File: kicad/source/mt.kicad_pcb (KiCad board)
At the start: 4 copper layers, 132 parts, among them IC1 MCP73831T-2ACI_OT, IC10 SN74HC148NSR, IC11 SN74HC148NSR, IC2 BQ29728DSER, IC3 TLV74333PDBVR, IC4 TLV9152IDR, IC5 MSPM0G3507SPMR, IC6 IS62WV1288BLL-55QLI, IC7 DAC082S085CIMMX_NOPB, IC8 SN74HC148NSR, IC9 SN74HC148NSR, J1 694106301002, J2 3557-2, J3 SJ1-3524N, J4 Conn_01x05_Pin, J5 Conn_01x09_Pin, J6 Conn_01x03_Pin, J7 Conn_01x03_Pin, J8 Conn_01x03_Pin, Q1 CSD16406Q3, Q2 CSD16406Q3, U1 1043

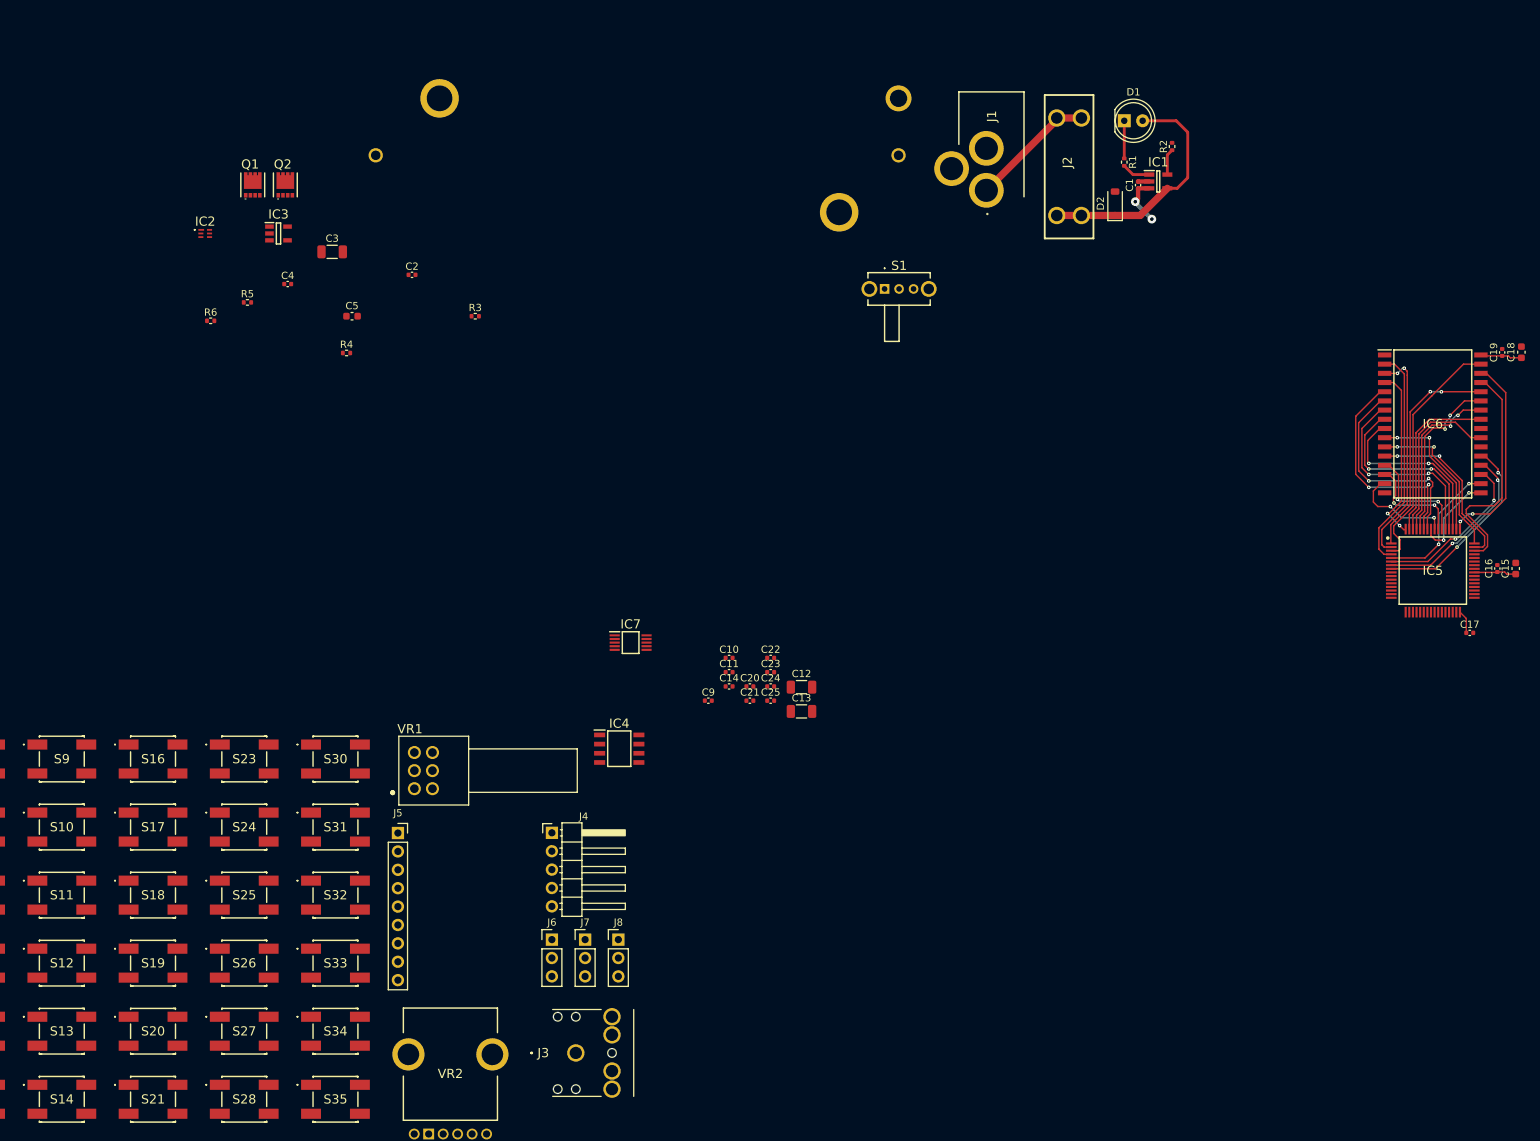
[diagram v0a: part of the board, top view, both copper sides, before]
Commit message: completed power electronics routing, fixed battery holder model
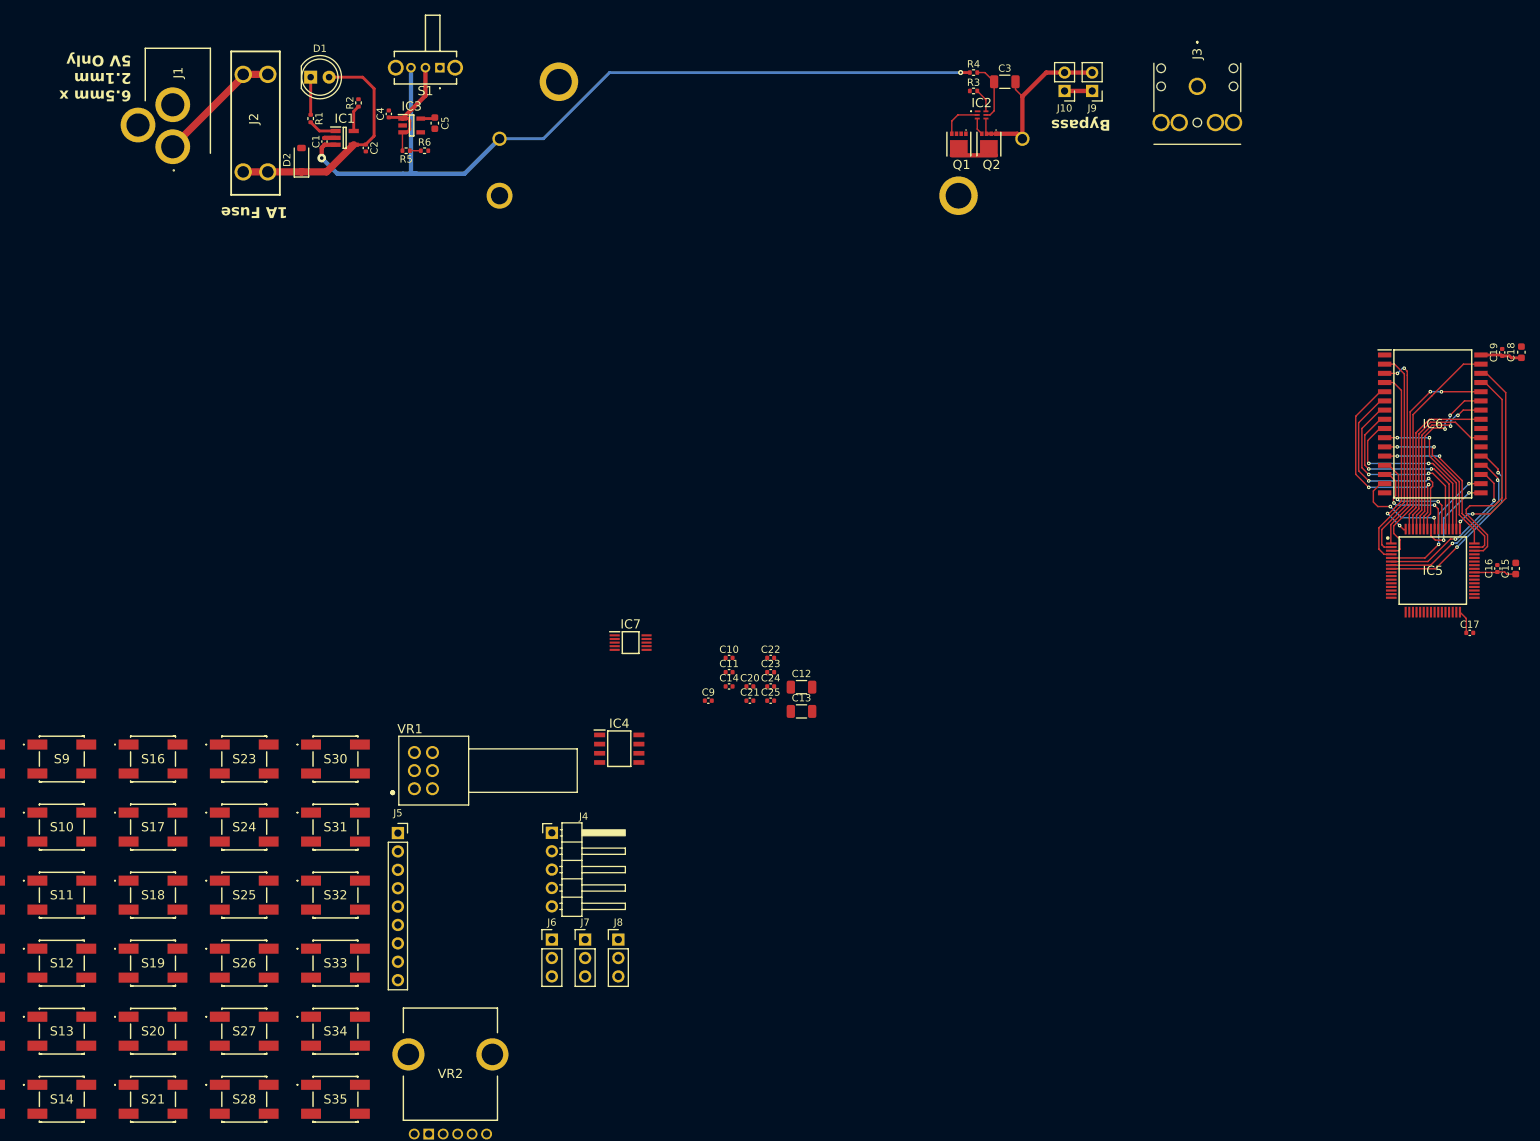
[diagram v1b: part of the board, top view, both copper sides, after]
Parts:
- added J10: Conn_01x02_Pin, Connector_PinHeader_2.54mm:PinHeader_1x02_P2.54mm_Vertical, F.Cu at (180.3, 23.5)
- added J9: Conn_01x02_Pin, Connector_PinHeader_2.54mm:PinHeader_1x02_P2.54mm_Vertical, F.Cu at (184.2, 23.5)
- moved J3 158.7 mm to (198.7, 22.9), turned to -90 degrees
- moved J1 112.5 mm to (53.4, 17.6)
- moved C1 112.5 mm to (78.1, 30.5)
- moved D1 112.5 mm to (76.2, 21.6)
- moved J2 112.5 mm to (68.6, 27.9)
- moved R1 112.5 mm to (76.2, 27.3)
- moved D2 112.5 mm to (74.9, 33.0)
- moved IC1 112.5 mm to (80.9, 30.0)
- moved R2 112.5 mm to (82.8, 25.1)
- moved IC2 108.5 mm to (168.9, 26.8)
- moved Q1 97.7 mm to (165.7, 30.8), turned to 180 degrees
- moved Q2 97.3 mm to (169.9, 30.8), turned to 180 degrees
- moved C3 95.8 mm to (172.1, 22.2)
- moved R4 94.9 mm to (167.8, 21.0)
- moved R3 75.5 mm to (167.8, 23.5)
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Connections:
- Q1 pad 9: Net-(Q1-D_1) -> (no net)
- Q2 pad 9: Net-(Q1-D_1) -> (no net)
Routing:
- net CELL+: track 6.88 -> 115.1 mm
- net Net-(IC2-VSS): track 0.00 -> 26.6 mm
- net Net-(IC3-EN): track 0.00 -> 16.4 mm
- net Net-(IC2-BAT): track 0.00 -> 8.25 mm
- net Net-(Q1-D_1): track 0.00 -> 6.10 mm
- net Net-(IC2-COUT): track 0.00 -> 5.62 mm
- net GND: track 1.56 -> 5.37 mm
- net Net-(IC2-V-): track 0.00 -> 3.31 mm
- net Net-(IC2-DOUT): track 0.00 -> 2.36 mm
- net VDD: track 11.6 -> 13.8 mm
- net VBAT: track 0.00 -> 1.52 mm
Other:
- board text added: "1A Fuse"
- board text added: "6.5mm x 2.1mm 5V Only"
- board text added: "Bypass"

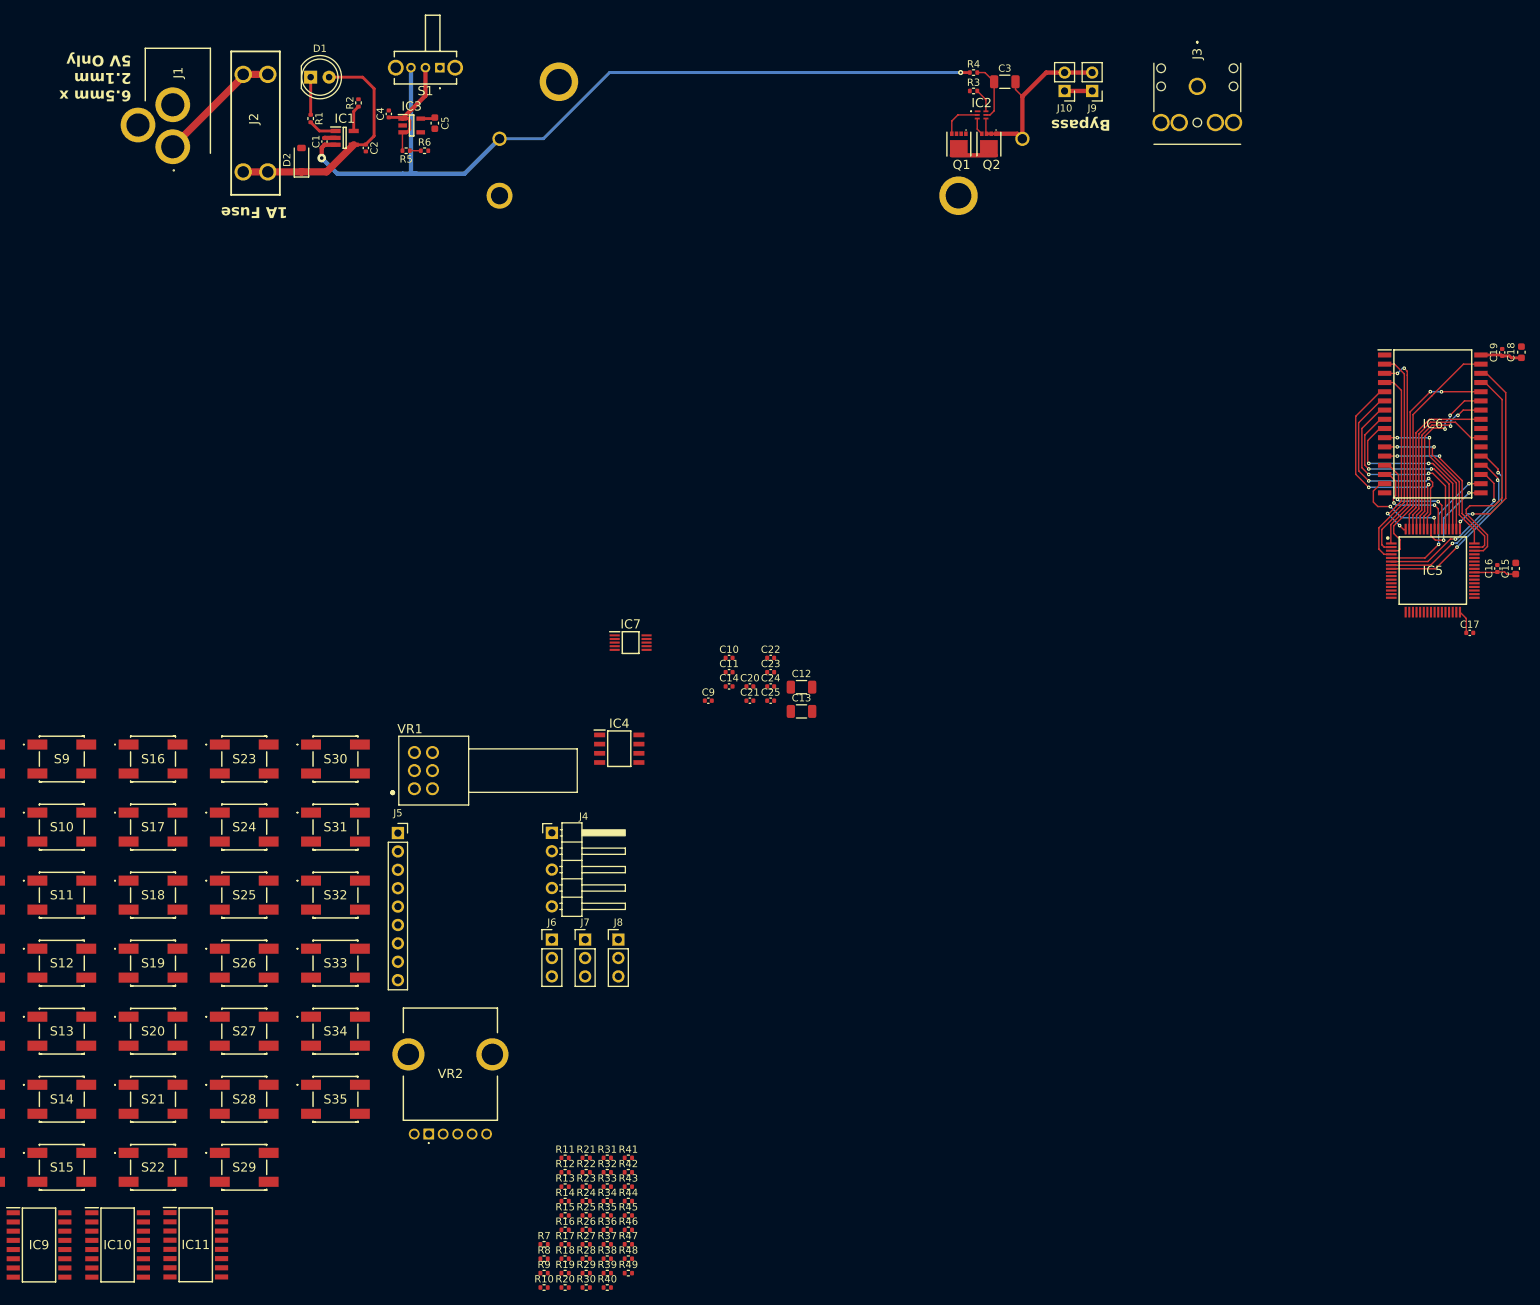
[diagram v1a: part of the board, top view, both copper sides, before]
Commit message: completed analog electronics routing
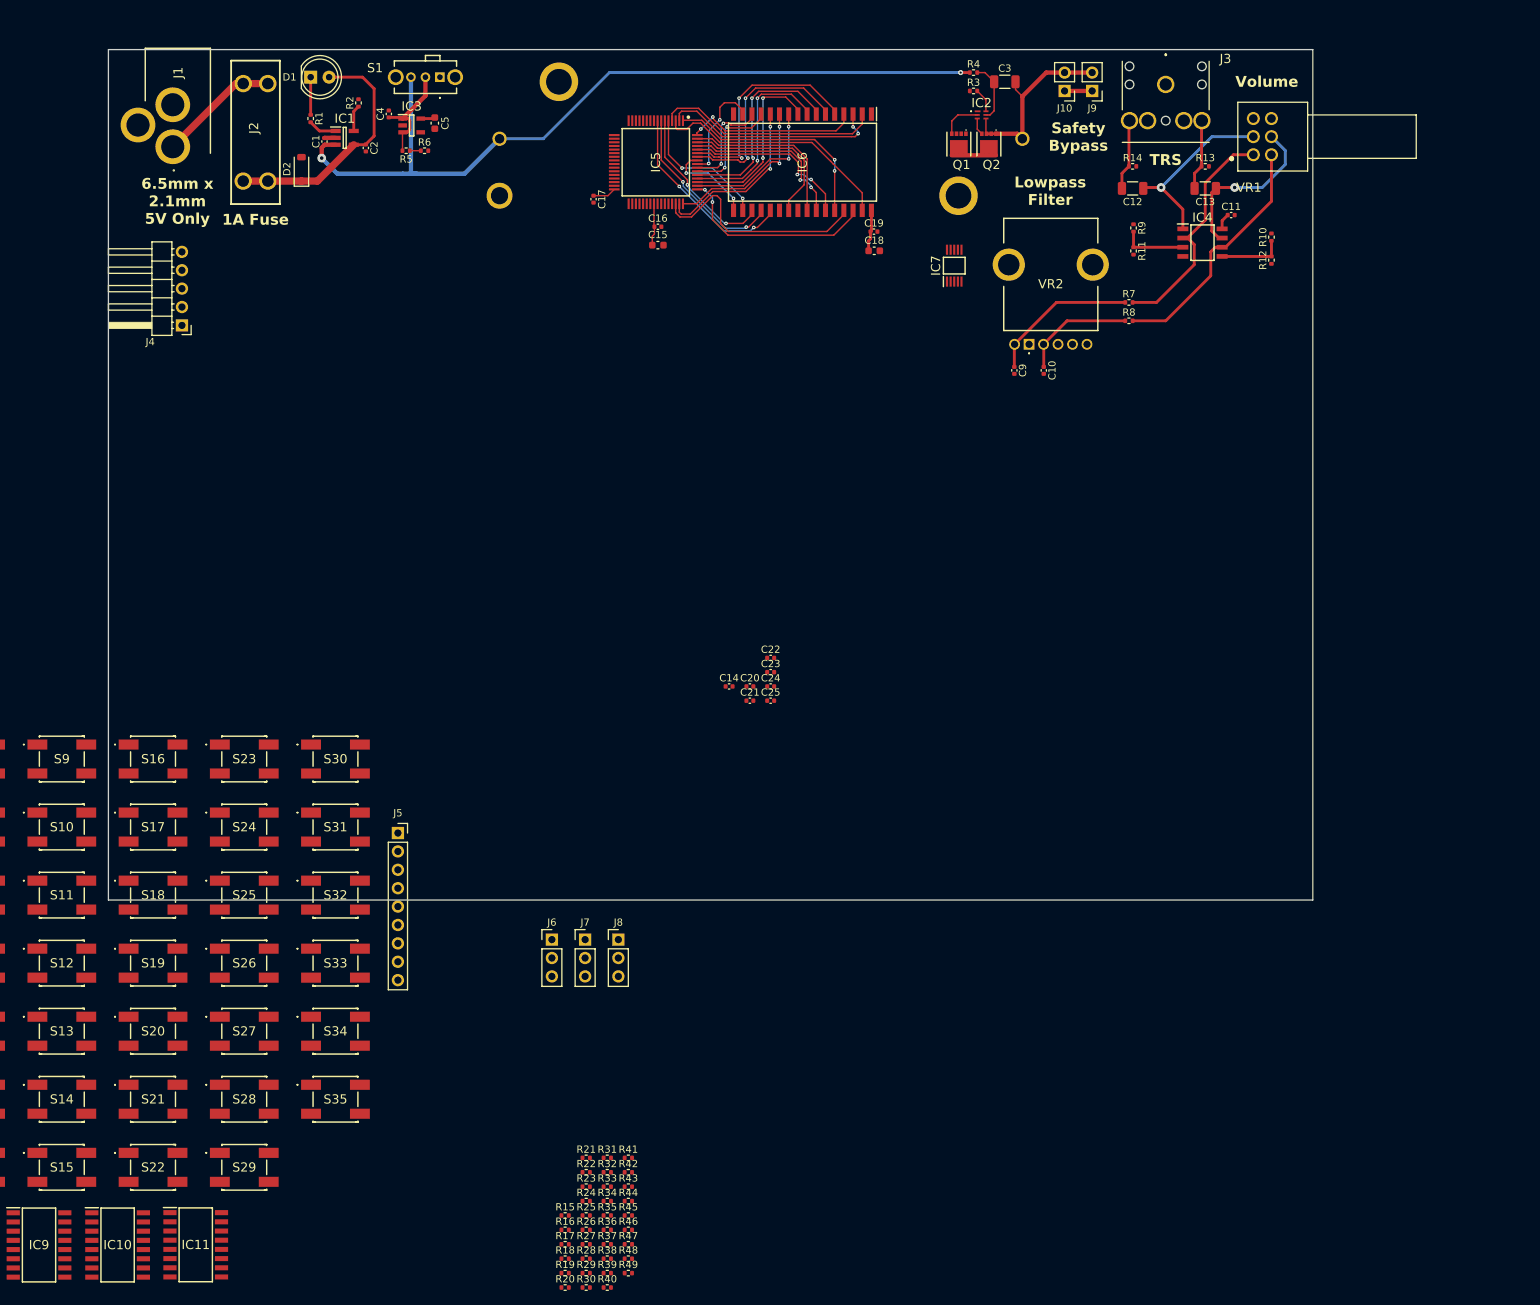
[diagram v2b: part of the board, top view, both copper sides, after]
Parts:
- moved R10 176.5 mm to (208.9, 43.7), turned to 90 degrees
- moved R13 166.4 mm to (199.8, 33.9)
- moved R9 165.8 mm to (189.9, 42.4), turned to -90 degrees
- moved R14 163.0 mm to (189.7, 33.9)
- moved R12 159.4 mm to (208.9, 46.9), turned to 90 degrees
- moved R7 153.1 mm to (189.2, 52.7)
- moved R8 152.7 mm to (189.2, 55.2)
- moved R11 147.8 mm to (189.9, 45.6), turned to -90 degrees
- moved VR1 145.3 mm to (206.4, 32.3)
- moved VR2 137.0 mm to (175.4, 58.5)
- moved C17 135.1 mm to (115.3, 38.4), turned to -90 degrees
- moved C15 126.6 mm to (124.2, 44.8), turned to 0 degrees
- moved C16 125.2 mm to (124.2, 42.3), turned to 0 degrees
- moved IC5 121.3 mm to (123.9, 33.3), turned to -90 degrees
- moved IC4 106.7 mm to (199.4, 44.5)
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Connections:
- R12 pad 1: Net-(IC4-IN2+) -> GND
- R12 pad 2: GND -> Net-(IC4-IN2+)
- R7 pad 1: RV1A -> Net-(C9-Pad1)
- R7 pad 2: Net-(C9-Pad1) -> RV1A
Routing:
- net RV2A: track 0.00 -> 34.4 mm
- net RV1A: track 0.00 -> 32.9 mm
- net L: track 0.00 -> 25.1 mm, vias 0 -> 1
- net R: track 0.00 -> 23.5 mm, vias 0 -> 1
- net Net-(C9-Pad1): track 0.00 -> 20.8 mm
- net Net-(C10-Pad1): track 0.00 -> 15.8 mm
- net Net-(J3-TIP): track 0.00 -> 9.80 mm
- net Net-(J3-RING): track 0.00 -> 9.78 mm
- net Net-(IC4-IN1+): track 0.00 -> 8.97 mm
- net Net-(IC4-IN2+): track 0.00 -> 8.97 mm
- net VDD: track 13.8 -> 16.0 mm
- net CELL+: track 115.1 -> 113.8 mm
- net Net-(IC3-EN): track 16.4 -> 15.1 mm
- net Net-(J1-POWER): track 17.4 -> 16.7 mm
- net Net-(D1-A): track 33.6 -> 34.1 mm
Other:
- board outline added: 166.4 x 117.5 mm
- board text added: "Lowpass Filter"
- board text added: "Safety Bypass"
- board text added: "TRS"
- board text added: "Volume"
- board text removed: "Bypass"

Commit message: completed peripherals routing, set up zone fills
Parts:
- added H1: MountingHole_Pad, MountingHole:MountingHole_3.2mm_M3_Pad_Via, F.Cu at (102.2, 53.3)
- added H2: MountingHole_Pad, MountingHole:MountingHole_3.2mm_M3_Pad_Via, F.Cu at (160.7, 53.3)
- added H3: MountingHole_Pad, MountingHole:MountingHole_3.2mm_M3_Pad_Via, F.Cu at (102.2, 104.1)
- added H4: MountingHole_Pad, MountingHole:MountingHole_3.2mm_M3_Pad_Via, F.Cu at (160.7, 104.1)
- moved C24 284.6 mm to (-50.0, 317.9)
- moved R16 253.9 mm to (-80.6, 14.6), turned to -90 degrees
- moved C23 245.1 mm to (-94.3, 176.5)
- moved R23 231.8 mm to (-47.6, 8.89), turned to -90 degrees
- moved C22 224.8 mm to (-82.2, 66.0)
- moved R17 211.3 mm to (-36.4, 31.8)
- moved R19 211.3 mm to (-36.4, 35.8)
- moved R20 211.3 mm to (-36.4, 37.8)
- moved R21 211.3 mm to (-33.5, 19.9)
- moved R18 211.3 mm to (-36.4, 33.8)
- moved R22 211.3 mm to (-33.5, 21.9)
- moved C25 209.0 mm to (110.1, 314.6)
- moved S34 200.5 mm to (250.0, 259.2)
- moved S35 200.5 mm to (250.0, 268.6)
- moved IC8 189.2 mm to (-122.6, 68.6)
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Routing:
- net SWDIO: track 0.00 -> 80.7 mm, vias 0 -> 2
- net SWCLK: track 0.00 -> 74.3 mm
- net SPI1_PICO: track 0.00 -> 44.4 mm
- net ~SYNC: track 0.00 -> 43.7 mm, vias 0 -> 2
- net SPI1_SCK: track 0.00 -> 42.3 mm
- net DACR: track 0.00 -> 32.2 mm, vias 0 -> 1
- net DACL: track 0.00 -> 31.0 mm, vias 0 -> 1
- net VBAT: track 1.52 -> 32.5 mm, vias 0 -> 2
- net SPI0_PICO: track 0.00 -> 30.1 mm, vias 0 -> 2
- net SPI0_SCK: track 0.00 -> 29.2 mm, vias 0 -> 2
- net SPI0_CS0: track 0.00 -> 27.8 mm, vias 0 -> 1
- net Net-(J5-Pin_7): track 0.00 -> 19.8 mm
- net Net-(J5-Pin_8): track 0.00 -> 14.7 mm
- net NRST: track 0.00 -> 12.3 mm
- net Net-(IC8-7): track 0.00 -> 10.7 mm
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- added copper zone on B.Cu, net GND
- added copper zone on F.Cu, net GND
- added copper zone on In1.Cu, net GND
- added copper zone on In2.Cu, net VDD
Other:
- board size 166.4 x 117.5 mm -> 166.4 x 127 mm
- board text added: "DISPLAY"
- board text added: "EXTIN"
- board text added: "EXTMODE"
- board text added: "GND"
- board text added: "NRST"
- board text added: "SWCLK"
- board text added: "SWDIO"
- board text added: "VDD"

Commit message: converted button ranks to hierarchical schematics, prepared button layout pattern
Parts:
- moved R40 322.0 mm to (-115.6, 116.8), turned to -90 degrees
- moved R44 311.7 mm to (-115.6, 132.1), turned to -90 degrees
- moved R41 303.0 mm to (-101.0, 116.8), turned to -90 degrees
- moved R45 299.5 mm to (-101.0, 132.1), turned to -90 degrees
- moved R42 291.2 mm to (-86.4, 116.8), turned to -90 degrees
- moved R46 287.6 mm to (-86.4, 132.1), turned to -90 degrees
- moved R32 283.1 mm to (-228.8, 105.4), turned to -90 degrees
- moved R43 279.8 mm to (-71.8, 116.8), turned to -90 degrees
- moved R36 278.9 mm to (-228.8, 120.7), turned to -90 degrees
- moved R47 276.0 mm to (-71.8, 132.1), turned to -90 degrees
- moved S26 274.2 mm to (-120.7, 121.9)
- moved R33 272.5 mm to (-214.2, 105.4), turned to -90 degrees
- moved R37 268.1 mm to (-214.2, 120.7), turned to -90 degrees
- moved S27 267.6 mm to (-106.0, 121.9)
- moved C25 264.7 mm to (-94.0, 146.1)
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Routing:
- net Net-(IC11-0): track 0.00 -> 10.0 mm
- net Net-(IC10-7): track 0.00 -> 10.0 mm
- net Net-(IC10-6): track 0.00 -> 10.0 mm
- net Net-(IC9-4): track 0.00 -> 10.0 mm
- net Net-(IC8-6): track 0.00 -> 10.0 mm
- net Net-(IC8-4): track 0.00 -> 10.0 mm
- net Net-(IC9-6): track 0.00 -> 10.0 mm
- net Net-(IC11-4): track 0.00 -> 10.0 mm
- net Net-(IC11-2): track 0.00 -> 10.0 mm
- net Net-(IC11-1): track 0.00 -> 10.0 mm
- net Net-(IC10-4): track 0.00 -> 10.0 mm
- net Net-(IC9-0): track 0.00 -> 10.0 mm
- net Net-(IC9-1): track 0.00 -> 10.0 mm
- net Net-(IC9-7): track 0.00 -> 10.0 mm
- net Net-(IC9-3): track 0.00 -> 10.0 mm
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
